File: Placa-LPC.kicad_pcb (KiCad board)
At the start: 2 copper layers, 120 x 90 mm, 45 parts, among them K3 CONN_3, P1 12V, P13 CONN_2, P3 CONN_6, P9 CONN_4, U1 LM2575-5.0, U3.1 NCP1117ST33T3G, X1 12MHz

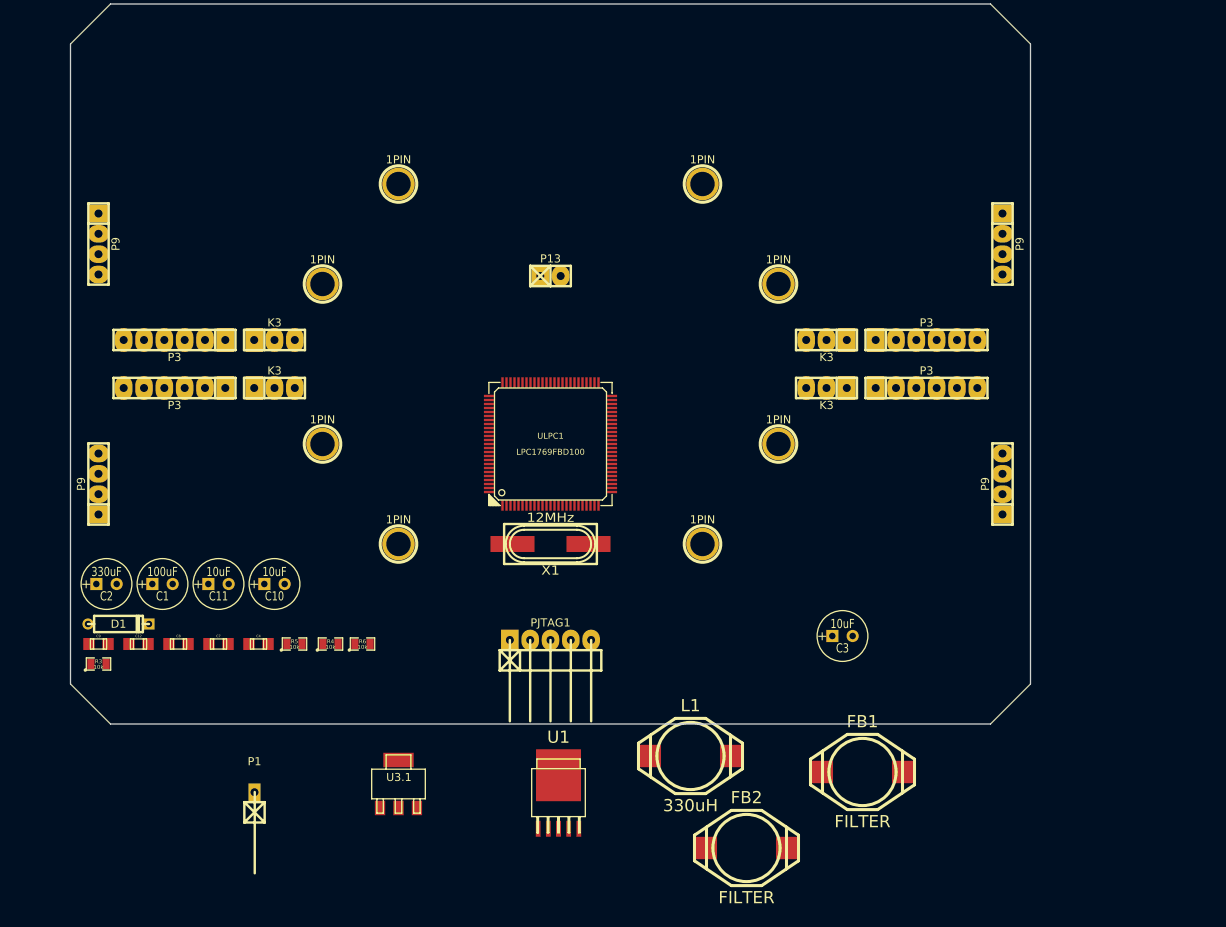
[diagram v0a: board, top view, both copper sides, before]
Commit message: Agrego modulos
Se agregaron las dimensiones de los modulos rf y mpu.
Faltan definir pines y rutear
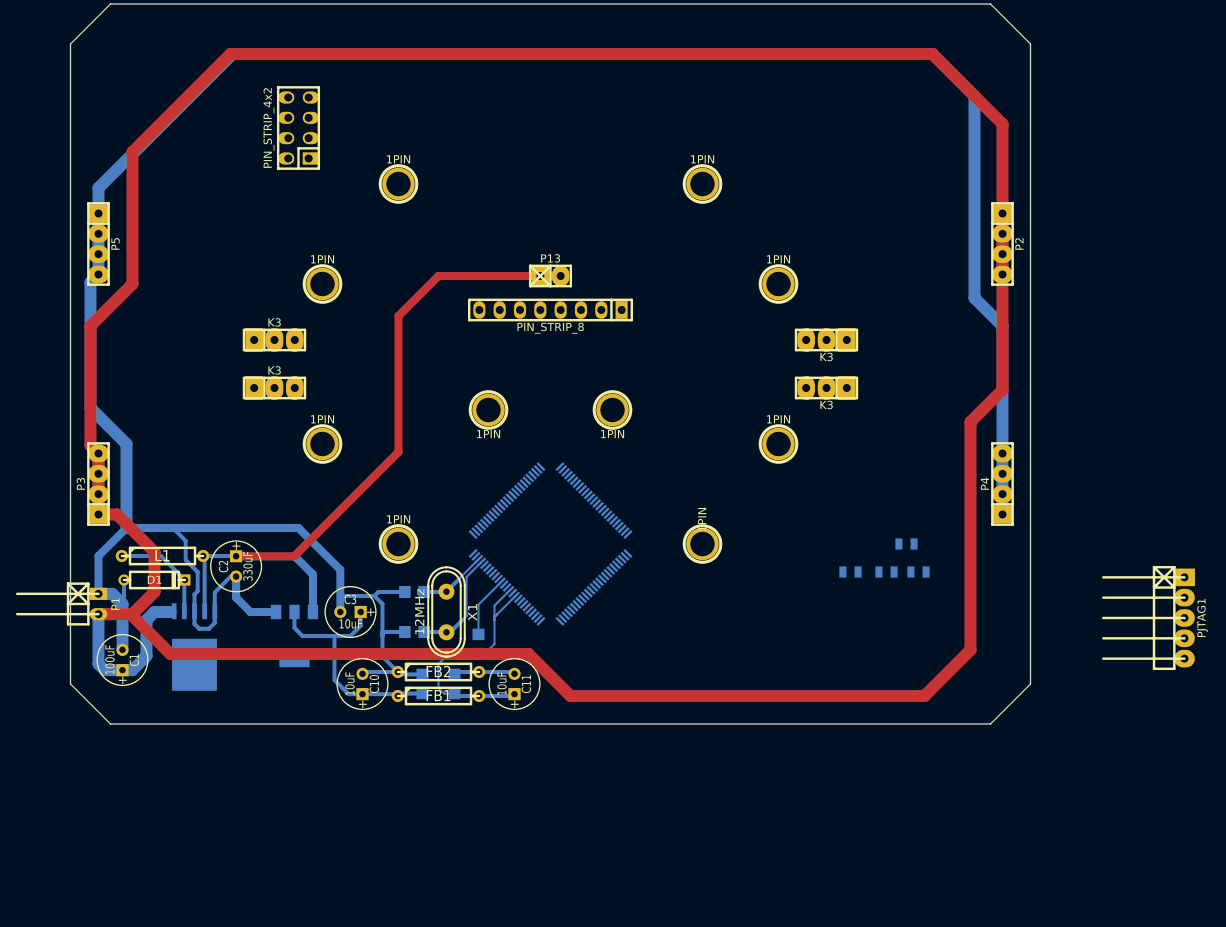
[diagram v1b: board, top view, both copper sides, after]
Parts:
- removed the P3 at (243.0, 124.0)
- removed the P3 at (243.0, 130.0)
- removed the P3 at (149.0, 124.0)
- removed the P3 at (149.0, 130.0)
- removed P9 (x4): CONN_4, pin_strip_4
- added 1PIN: P***, 1pin, F.Cu at (203.8, 132.8)
- added 1PIN: P***, 1pin, F.Cu at (188.2, 132.8)
- added P2: CONN_4, pin_strip_4, F.Cu at (252.5, 112.0)
- added P3: CONN_4, pin_strip_4, F.Cu at (139.5, 142.0)
- added P4: CONN_4, pin_strip_4, F.Cu at (252.5, 142.0)
- added P5: CONN_4, pin_strip_4, F.Cu at (139.5, 112.0)
- added PIN_STRIP_4x2: Val**, pin_strip_4x2, F.Cu at (164.5, 97.5)
- added PIN_STRIP_8: Val**, pin_strip_8, F.Cu at (196.0, 120.2)
- C12, C4, C7, C8, C9, R3, R4, R5, R6, U1, U3.1, ULPC1: moved to B.Cu
- FB1, FB2, L1: footprint inductor_smd_do3316p -> R4
- P1: footprint pin_strip_1-90 -> pin_strip_2-90
- X1: footprint crystal_hc-49/smd -> crystal_hc-49s
- moved R3 102.1 mm to (240.5, 149.5)
- moved PJTAG1 79.3 mm to (275.2, 158.8), turned to 270 degrees
- moved L1 70.6 mm to (147.5, 151.0)
- moved R4 70.1 mm to (238.0, 153.0)
- moved R5 70.1 mm to (233.5, 153.0)
- moved R6 70.1 mm to (242.0, 153.0)
- moved C3 61.6 mm to (171.0, 158.0), turned to 180 degrees
- moved FB1 53.8 mm to (182.0, 168.5)
- moved U1 50.1 mm to (151.5, 161.0)
- moved FB2 44.3 mm to (182.0, 165.5)
- moved C12 42.5 mm to (187.0, 162.0), turned to 90 degrees
- moved C9 40.8 mm to (180.0, 167.0), turned to 90 degrees
- moved C11 39.1 mm to (191.5, 167.0), turned to 90 degrees
- moved P1 30.5 mm to (139.5, 157.0), turned to 270 degrees
- moved C8 30.2 mm to (179.0, 155.5)
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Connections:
- C1 pad 1: N-0000088 (its old number) -> N-0000089
- P13 pad 1: V_5v -> +5V
- P13 pad 2: V_5v -> +5V
- U1 pad 1: N-0000088 (its old number) -> N-0000089
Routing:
- net N-0000089: track 0.00 -> 402.7 mm
- net GND: track 0.00 -> 363.9 mm
- net +5V: track 0.00 -> 93.9 mm
- net +3.3VADC: track 0.00 -> 33.1 mm
- net +3.3V: track 0.00 -> 30.4 mm
- net GNDA: track 0.00 -> 15.5 mm
- net N-0000086: track 0.00 -> 13.7 mm
- net N-0000088: track 0.00 -> 13.1 mm
- net N-0000087: track 0.00 -> 8.58 mm
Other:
- net class Default: clearance 0.254 -> 0.2
- rule trace_clearance: 0.254 -> 0.2

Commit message: Definicion de pines
Definicion de algunos pines y ruteado de algunas pistas.
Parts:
- removed the K3 at (161.5, 130.0)
- removed PIN_STRIP_4x2: Val**, pin_strip_4x2
- removed PIN_STRIP_8: Val**, pin_strip_8
- added K1: CONN_3, pin_strip_3, F.Cu at (161.5, 130.0)
- added P6: CONN_4X2, pin_strip_4x2, F.Cu at (222.0, 97.2)
- added P7: CONN_8, pin_strip_8, F.Cu at (196.0, 120.2)
- added P8: CONN_6, pin_strip_6, F.Cu at (149.0, 130.0)
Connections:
- ULPC1 pad 32: (no net) -> N-0000021
- ULPC1 pad 33: (no net) -> N-0000030
- ULPC1 pad 34: (no net) -> N-0000020
- ULPC1 pad 35: (no net) -> N-0000026
- ULPC1 pad 36: (no net) -> N-0000019
- ULPC1 pad 37: (no net) -> N-0000018
- ULPC1 pad 38: (no net) -> N-0000017
- ULPC1 pad 39: (no net) -> N-0000023
- ULPC1 pad 40: (no net) -> N-0000028
- ULPC1 pad 45: (no net) -> N-0000027
- ULPC1 pad 46: (no net) -> N-0000022
- ULPC1 pad 47: (no net) -> N-0000016
- ULPC1 pad 76: (no net) -> N-0000025
- ULPC1 pad 77: (no net) -> N-0000013
- ULPC1 pad 78: (no net) -> N-0000014
- ULPC1 pad 79: (no net) -> N-0000029
- ULPC1 pad 80: (no net) -> N-0000015
- ULPC1 pad 81: (no net) -> N-0000024
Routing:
- net N-0000015: track 0.00 -> 69.5 mm
- net N-0000021: track 0.00 -> 54.4 mm
- net N-0000030: track 0.00 -> 51.3 mm
- net N-0000020: track 0.00 -> 48.7 mm
- net N-0000026: track 0.00 -> 46.1 mm
- net N-0000019: track 0.00 -> 43.9 mm
- net N-0000018: track 0.00 -> 41.5 mm
- net N-0000017: track 0.00 -> 38.6 mm
- net N-0000023: track 0.00 -> 35.7 mm
- net N-0000028: track 0.00 -> 33.1 mm
- net N-0000027: track 0.00 -> 26.1 mm
- net N-0000016: track 0.00 -> 24.8 mm
- net N-0000022: track 0.00 -> 24.4 mm

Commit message: Actualizado desde mi pc
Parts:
- moved C1 127.1 mm to (246.0, 90.2), turned to 270 degrees
- moved P1 124.7 mm to (249.0, 97.2), turned to 90 degrees
- moved D1 109.6 mm to (242.0, 100.2), turned to 180 degrees
- moved U1 109.1 mm to (237.0, 93.2), turned to 180 degrees
- moved L1 105.0 mm to (241.0, 103.2), turned to 180 degrees
- moved R3 93.7 mm to (314.2, 91.8)
- moved R4 93.7 mm to (311.8, 95.2)
- moved R5 93.7 mm to (307.2, 95.2)
- moved R6 93.7 mm to (315.8, 95.2)
- moved C10 90.9 mm to (216.0, 87.2), turned to 270 degrees
- moved U3.1 90.8 mm to (224.5, 93.2), turned to 180 degrees
- moved C2 90.4 mm to (231.8, 102.0), turned to 90 degrees
- moved FB1 86.3 mm to (206.4, 85.7), turned to 180 degrees
- moved C9 84.7 mm to (208.4, 87.2), turned to 270 degrees
- moved C4 82.4 mm to (204.4, 87.2), turned to 270 degrees
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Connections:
- K1 pad 1: N-0000017 -> N-0000022
- K1 pad 3: N-0000028 -> N-0000024
- P8 pad 1: N-0000021 -> N-0000019
- P8 pad 2: N-0000030 -> N-0000016
- P8 pad 3: N-0000020 -> N-0000017
- P8 pad 4: N-0000026 -> N-0000018
- P8 pad 5: N-0000019 -> N-0000020
- P8 pad 6: N-0000018 -> N-0000021
- ULPC1 pad 24: (no net) -> N-0000019
- ULPC1 pad 25: (no net) -> N-0000016
- ULPC1 pad 26: (no net) -> N-0000017
- ULPC1 pad 27: (no net) -> N-0000018
- ULPC1 pad 29: (no net) -> N-0000020
- ULPC1 pad 30: (no net) -> N-0000021
- ULPC1 pad 32: N-0000021 -> N-0000022
- ULPC1 pad 33: N-0000030 -> N-0000023
- ULPC1 pad 34: N-0000020 -> N-0000024
- ULPC1 pad 35: N-0000026 -> N-0000025
- ULPC1 pad 36: N-0000019 -> N-0000027
- ULPC1 pad 37: N-0000018 -> N-0000028
- ULPC1 pad 38: N-0000017 -> N-0000029
- ULPC1 pad 39: N-0000023 -> N-0000030
- ULPC1 pad 40: N-0000028 -> N-0000031
- ULPC1 pad 43: (no net) -> N-0000032
- ULPC1 pad 44: (no net) -> N-0000033
- ULPC1 pad 48: (no net) -> N-0000026
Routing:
- net N-0000092: track 402.7 -> 38.7 mm
- net GND: track 363.9 -> 154.7 mm
- net N-0000013: track 69.5 -> 0.00 mm
- net +5V: track 93.9 -> 28.9 mm
- net N-0000016: track 0.00 -> 56.4 mm
- net N-0000030: track 51.3 -> 0.00 mm
- net N-0000026: track 46.1 -> 0.00 mm
- net N-0000022: track 0.00 -> 37.1 mm
- net N-0000028: track 33.1 -> 0.00 mm
- net N-0000024: track 0.00 -> 31.6 mm
- net N-000008: track 0.00 -> 29.8 mm
- net N-000002: track 0.00 -> 27.4 mm
- net N-0000019: track 43.9 -> 59.8 mm
- net +3.3VADC: track 33.1 -> 19.7 mm
- net N-0000017: track 38.6 -> 50.0 mm
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
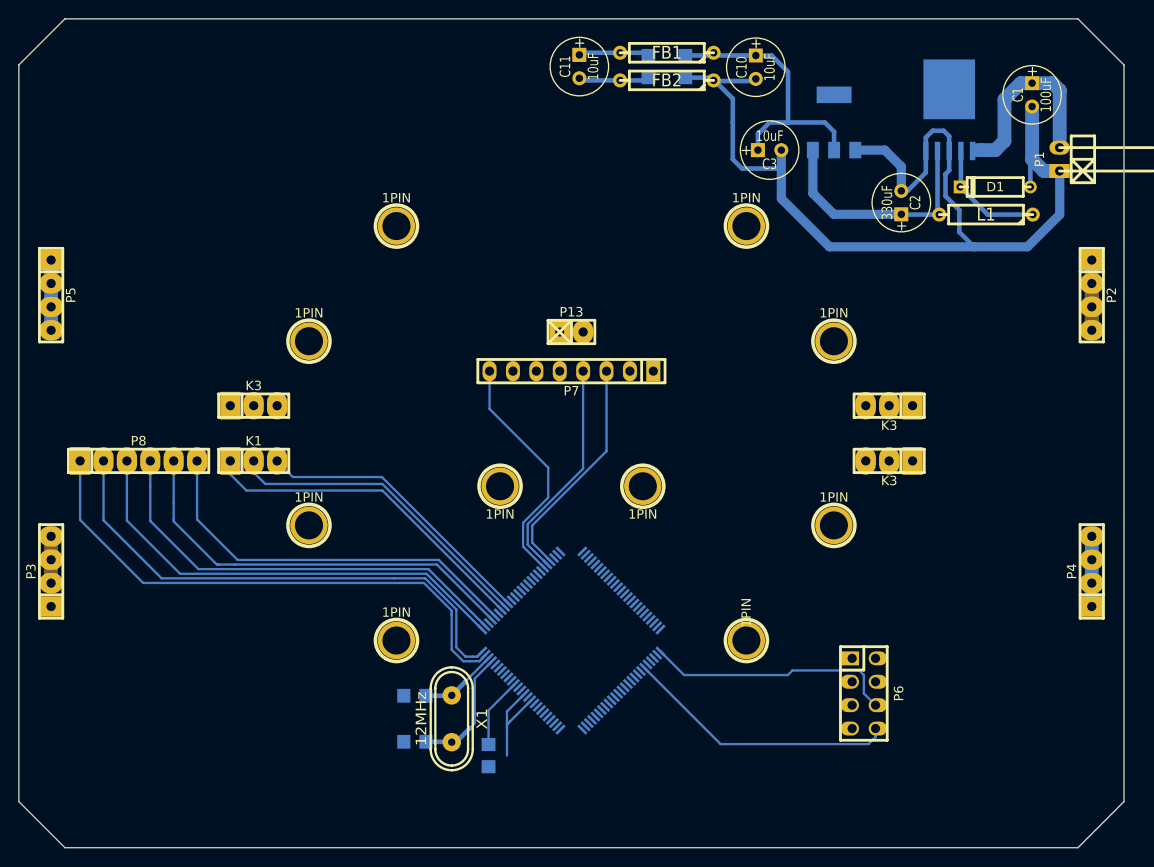
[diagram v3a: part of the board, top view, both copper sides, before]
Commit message: Ruteo pines
Ruteo completo de pines motor y módulos.
Falta pines programación y pines adc para batería.
Falta definir conectores.
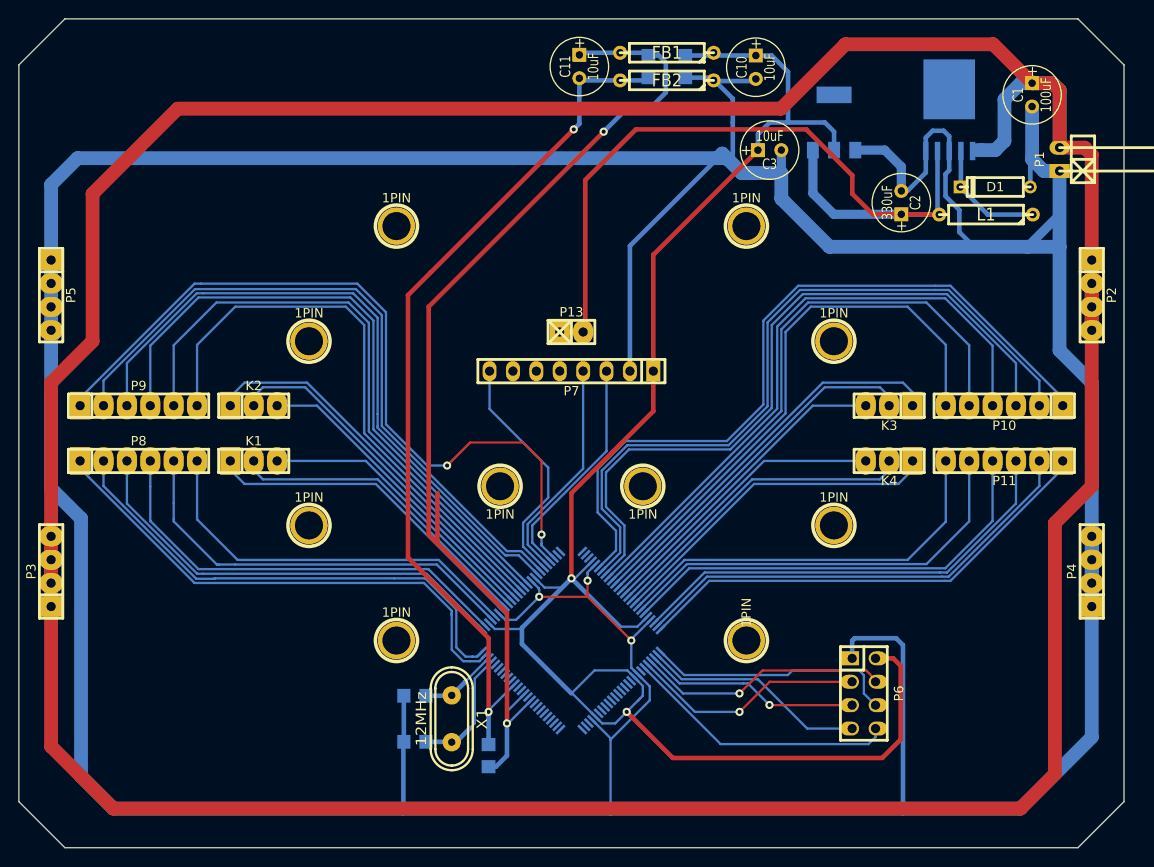
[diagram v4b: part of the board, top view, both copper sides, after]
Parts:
- removed the K3 at (230.5, 130.0)
- removed the K3 at (161.5, 124.0)
- added K2: CONN_3, pin_strip_3, F.Cu at (161.5, 124.0)
- added K4: CONN_3, pin_strip_3, F.Cu at (230.5, 130.0)
- added P10: CONN_6, pin_strip_6, F.Cu at (243.0, 124.0)
- added P11: CONN_6, pin_strip_6, F.Cu at (243.0, 130.0)
- added P9: CONN_6, pin_strip_6, F.Cu at (149.0, 124.0)
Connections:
- K3 pad 1: /Detector_Cruce/Zero33 -> N-0000022
- K3 pad 2: /Detector_Cruce/Zero31 -> N-0000014
- K3 pad 3: /Detector_Cruce/Zero32 -> N-0000015
- ULPC1 pad 56: (no net) -> N-0000025
- ULPC1 pad 57: (no net) -> N-0000028
- ULPC1 pad 58: (no net) -> N-0000029
- ULPC1 pad 59: (no net) -> N-0000019
- ULPC1 pad 60: (no net) -> N-0000020
- ULPC1 pad 61: (no net) -> N-0000021
- ULPC1 pad 62: (no net) -> N-0000022
- ULPC1 pad 63: (no net) -> N-0000014
- ULPC1 pad 64: (no net) -> N-0000015
- ULPC1 pad 65: (no net) -> N-0000035
- ULPC1 pad 66: (no net) -> N-0000037
- ULPC1 pad 67: (no net) -> N-0000036
- ULPC1 pad 68: (no net) -> N-0000038
- ULPC1 pad 69: (no net) -> N-0000031
- ULPC1 pad 70: (no net) -> N-0000032
- ULPC1 pad 73: (no net) -> N-0000033
- ULPC1 pad 74: (no net) -> N-0000030
- ULPC1 pad 75: (no net) -> N-0000034
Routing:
- net GND: track 154.7 -> 624.3 mm, vias 0 -> 3
- net N-0000092: track 38.7 -> 405.4 mm
- net +3.3V: track 30.4 -> 219.3 mm, vias 0 -> 2
- net +3.3VADC: track 19.7 -> 122.5 mm, vias 0 -> 2
- net N-000008: track 0.00 -> 84.3 mm, vias 0 -> 2
- net GNDA: track 15.5 -> 99.3 mm, vias 0 -> 2
- net N-0000025: track 0.00 -> 82.3 mm
- net N-0000028: track 0.00 -> 80.3 mm
- net N-0000029: track 0.00 -> 78.3 mm
- net N-000009: track 0.00 -> 74.0 mm
- net N-0000027: track 0.00 -> 72.0 mm
- net N-0000023: track 0.00 -> 69.5 mm
- net N-0000019: track 0.00 -> 68.1 mm
- net N-0000045: track 0.00 -> 66.3 mm
- net N-0000020: track 0.00 -> 65.0 mm
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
